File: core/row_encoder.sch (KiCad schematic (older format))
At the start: 16 parts

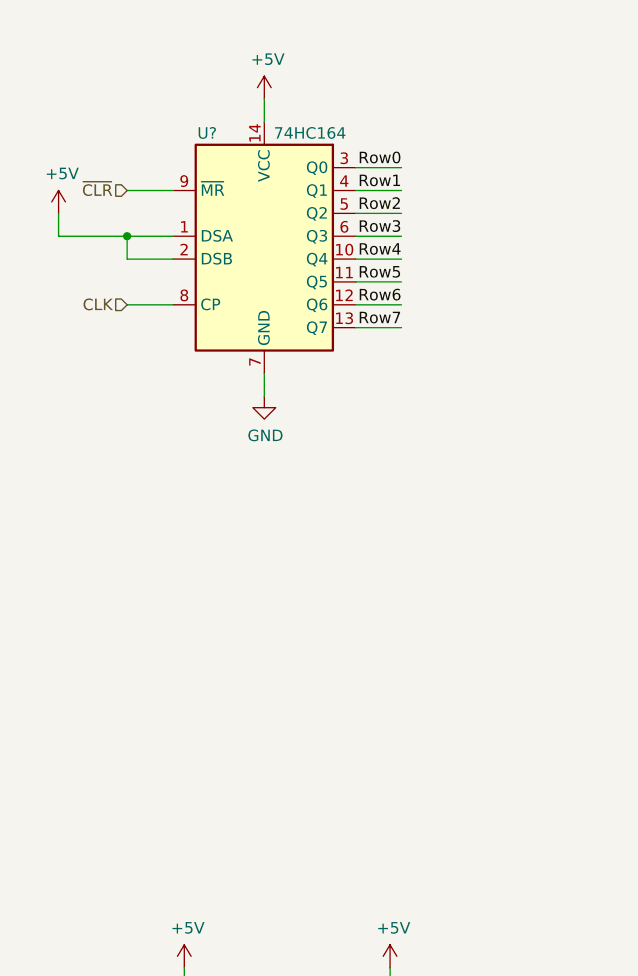
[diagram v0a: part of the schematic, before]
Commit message: Added NOR gate to shift register input to create a ring counter
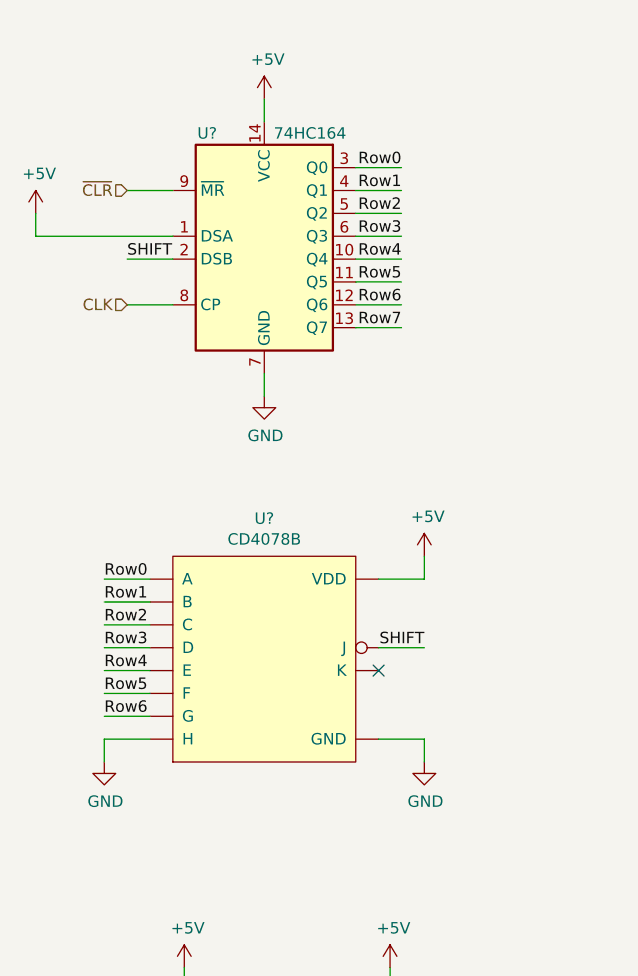
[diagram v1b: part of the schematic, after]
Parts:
- added U?: CD4078B, Package_SO:SOIC-14_3.9x8.7mm_P1.27mm, symbol keyboard_project:CD4078B
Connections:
- net +5V: now also U?.14 (VDD); no longer U?.2 (DSB)
- net GND: now also U?.12 (H), U?.7 (GND)
- net Row0: now also U?.2 (A)
- net Row1: now also U?.3 (B)
- net Row2: now also U?.4 (C)
- net Row3: now also U?.5 (D)
- net Row4: now also U?.9 (E)
- net Row5: now also U?.10 (F)
- net Row6: now also U?.11 (G)
- new net SHIFT: U?.13 (J), U?.2 (DSB)
- no-connect marks 6 -> 7
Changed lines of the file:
@@
 Wire Wire Line
 	3000 2900 2800 2900
-Wire Wire Line
-	3000 3100 2800 3100
-Wire Wire Line
-	2800 3100 2800 3200
-Wire Wire Line
-	2800 3200 3000 3200
-Wire Wire Line
-	2800 3100 2500 3100
-Connection ~ 2800 3100
 $Comp
-L power:+5V #PWR?
-U 1 1 5DC980CA
-P 2500 3000
-F 0 "#PWR?" H 2500 2850 50  0001 C CNN
-F 1 "+5V" H 2515 3173 50  0000 C CNN
-F 2 "" H 2500 3000 50  0001 C CNN
-F 3 "" H 2500 3000 50  0001 C CNN
-	1    2500 3000
+L keyboard_project:CD4078B U?
+U 1 1 5DCCD170
+P 3400 4950
+F 0 "U?" H 3400 5565 50  0000 C CNN
+F 1 "CD4078B" H 3400 5474 50  0000 C CNN
+F 2 "Package_SO:SOIC-14_3.9x8.7mm_P1.27mm" H 3400 4350 50  0001 C CNN
+F 3 "https://www.ti.com/lit/ds/symlink/cd4078b.pdf" H 3100 5450 50  0001 C CNN
+	1    3400 4950
 	1    0    0    -1
 $EndComp
 Wire Wire Line
-	2500 3100 2500 3000
+	2900 5200 2700 5200
+Wire Wire Line
+	2900 5100 2700 5100
+Wire Wire Line
+	2900 5000 2700 5000
+Wire Wire Line
+	2900 4900 2700 4900
+Wire Wire Line
+	2900 4800 2700 4800
+Wire Wire Line
+	2900 4700 2700 4700
+Wire Wire Line
+	2900 4600 2700 4600
+Text Label 2700 4600 0    50   ~ 0
+Row0
+Text Label 2700 4700 0    50   ~ 0
+Row1
+Text Label 2700 4800 0    50   ~ 0
+Row2
+Text Label 2700 4900 0    50   ~ 0
+Row3
+Text Label 2700 5000 0    50   ~ 0
+Row4
+Text Label 2700 5100 0    50   ~ 0
+Row5
+Text Label 2700 5200 0    50   ~ 0
+Row6
+Wire Wire Line
+	4100 4600 4100 4500
+Wire Wire Line
+	4100 5300 4100 5400
+NoConn ~ 3900 5000
+Wire Wire Line
+	3900 4900 4100 4900
+Wire Wire Line
+	3900 4600 4100 4600
+Wire Wire Line
+	3900 5300 4100 5300
+$Comp
+L power:+5V #PWR?
+U 1 1 5DCED549
+P 4100 4500
+F 0 "#PWR?" H 4100 4350 50  0001 C CNN
+F 1 "+5V" H 4115 4673 50  0000 C CNN
+F 2 "" H 4100 4500 50  0001 C CNN
+F 3 "" H 4100 4500 50  0001 C CNN
+	1    4100 4500
+	1    0    0    -1
+$EndComp
+$Comp
+L power:GND #PWR?
+U 1 1 5DCF0662
+P 4100 5400
+F 0 "#PWR?" H 4100 5150 50  0001 C CNN
+F 1 "GND" H 4105 5227 50  0000 C CNN
+F 2 "" H 4100 5400 50  0001 C CNN
+F 3 "" H 4100 5400 50  0001 C CNN
+	1    4100 5400
+	1    0    0    -1
+$EndComp
+Text Label 4100 4900 2    50   ~ 0
+SHIFT
+Wire Wire Line
+	2900 5300 2700 5300
+Wire Wire Line
+	2700 5300 2700 5400
+$Comp
+L power:GND #PWR?
+U 1 1 5DCF9F09
+P 2700 5400
+F 0 "#PWR?" H 2700 5150 50  0001 C CNN
+F 1 "GND" H 2705 5227 50  0000 C CNN
+F 2 "" H 2700 5400 50  0001 C CNN
+F 3 "" H 2700 5400 50  0001 C CNN
+	1    2700 5400
+	1    0    0    -1
+$EndComp
+Wire Wire Line
+	3000 3100 2400 3100
+Wire Wire Line
+	2400 3100 2400 3000
+$Comp
+L power:+5V #PWR?
+U 1 1 5DD01300
+P 2400 3000
+F 0 "#PWR?" H 2400 2850 50  0001 C CNN
+F 1 "+5V" H 2415 3173 50  0000 C CNN
+F 2 "" H 2400 3000 50  0001 C CNN
+F 3 "" H 2400 3000 50  0001 C CNN
+	1    2400 3000
+	1    0    0    -1
+$EndComp
+Wire Wire Line
+	3000 3200 2800 3200
+Text Label 2800 3200 0    50   ~ 0
+SHIFT
 $EndSCHEMATC

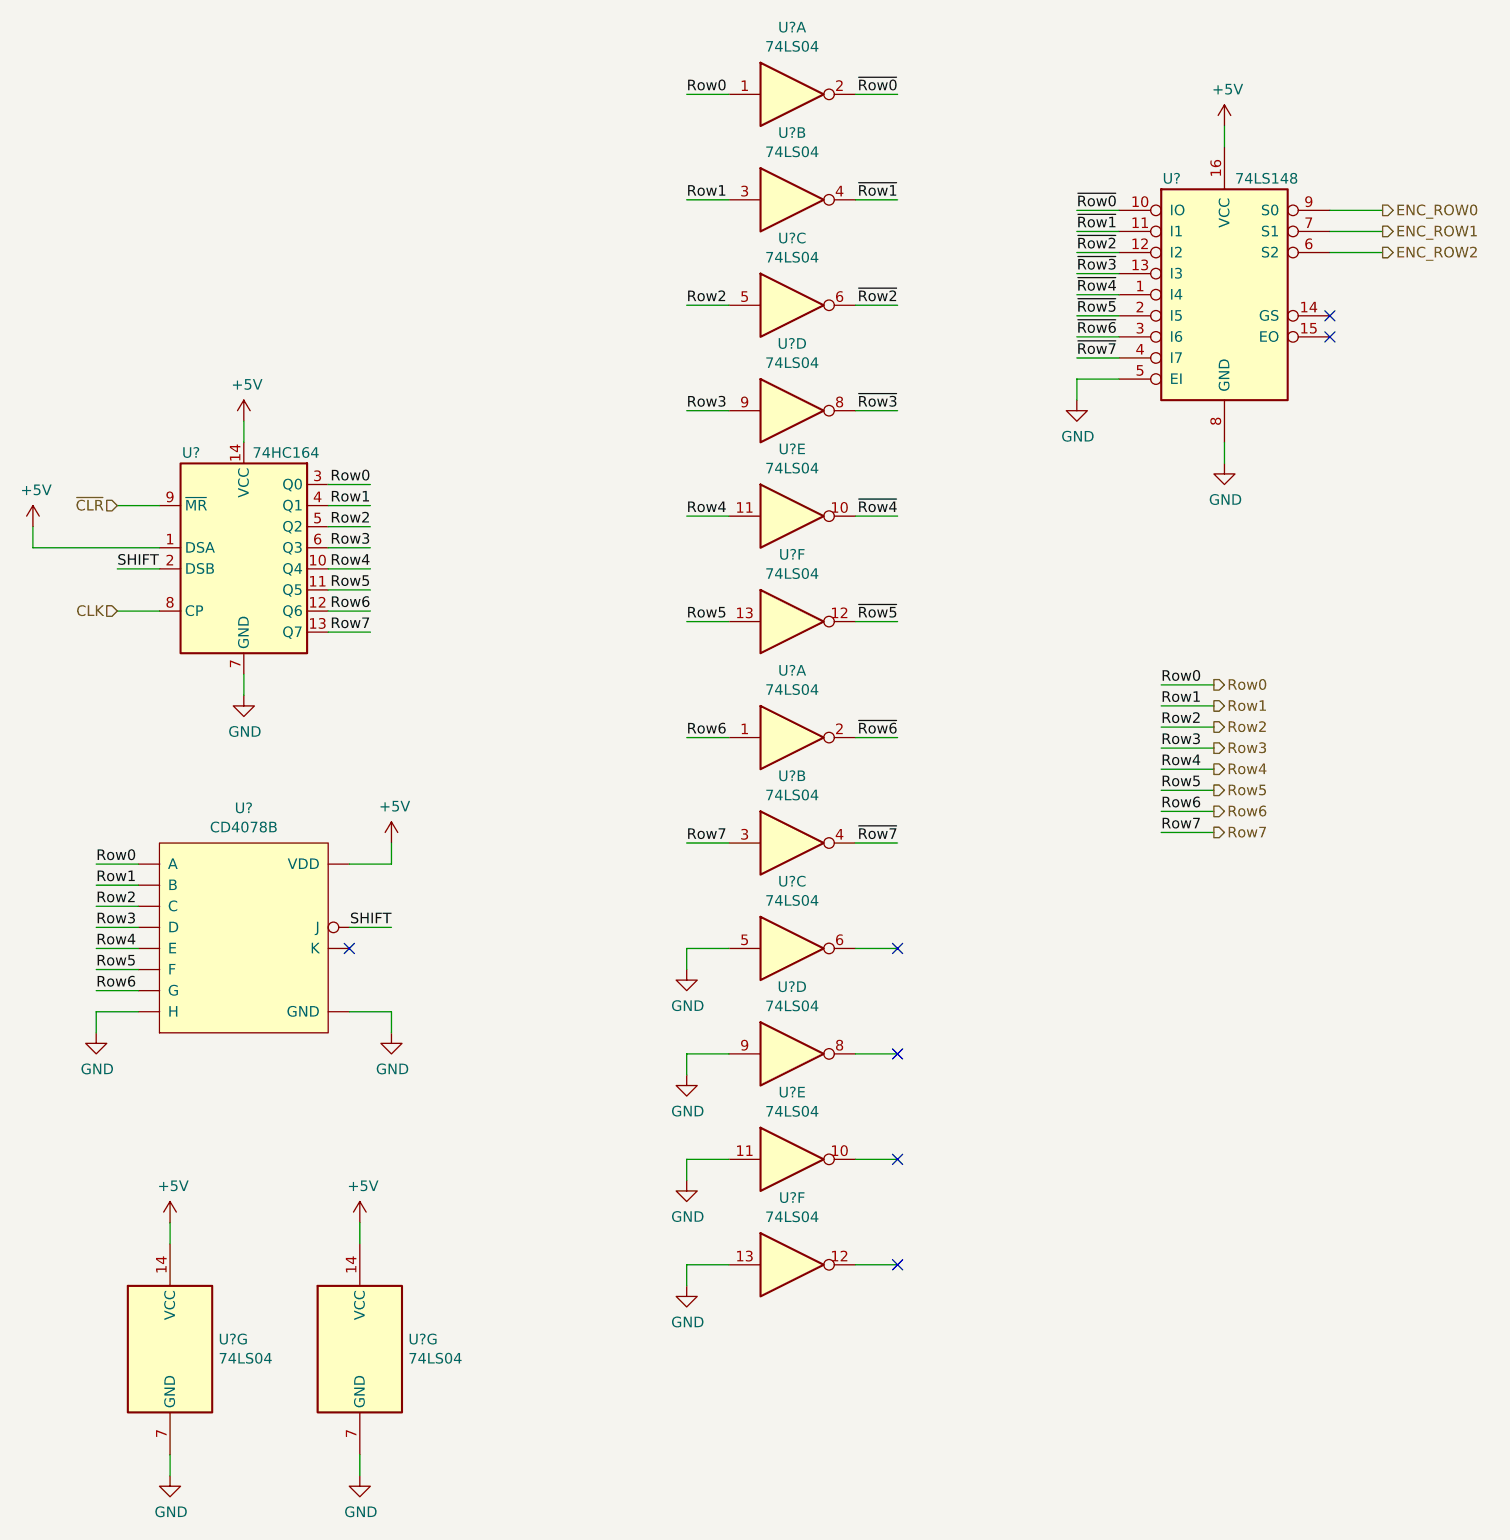
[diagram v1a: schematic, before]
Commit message: Changed encoder to CD4532B, removed inverters
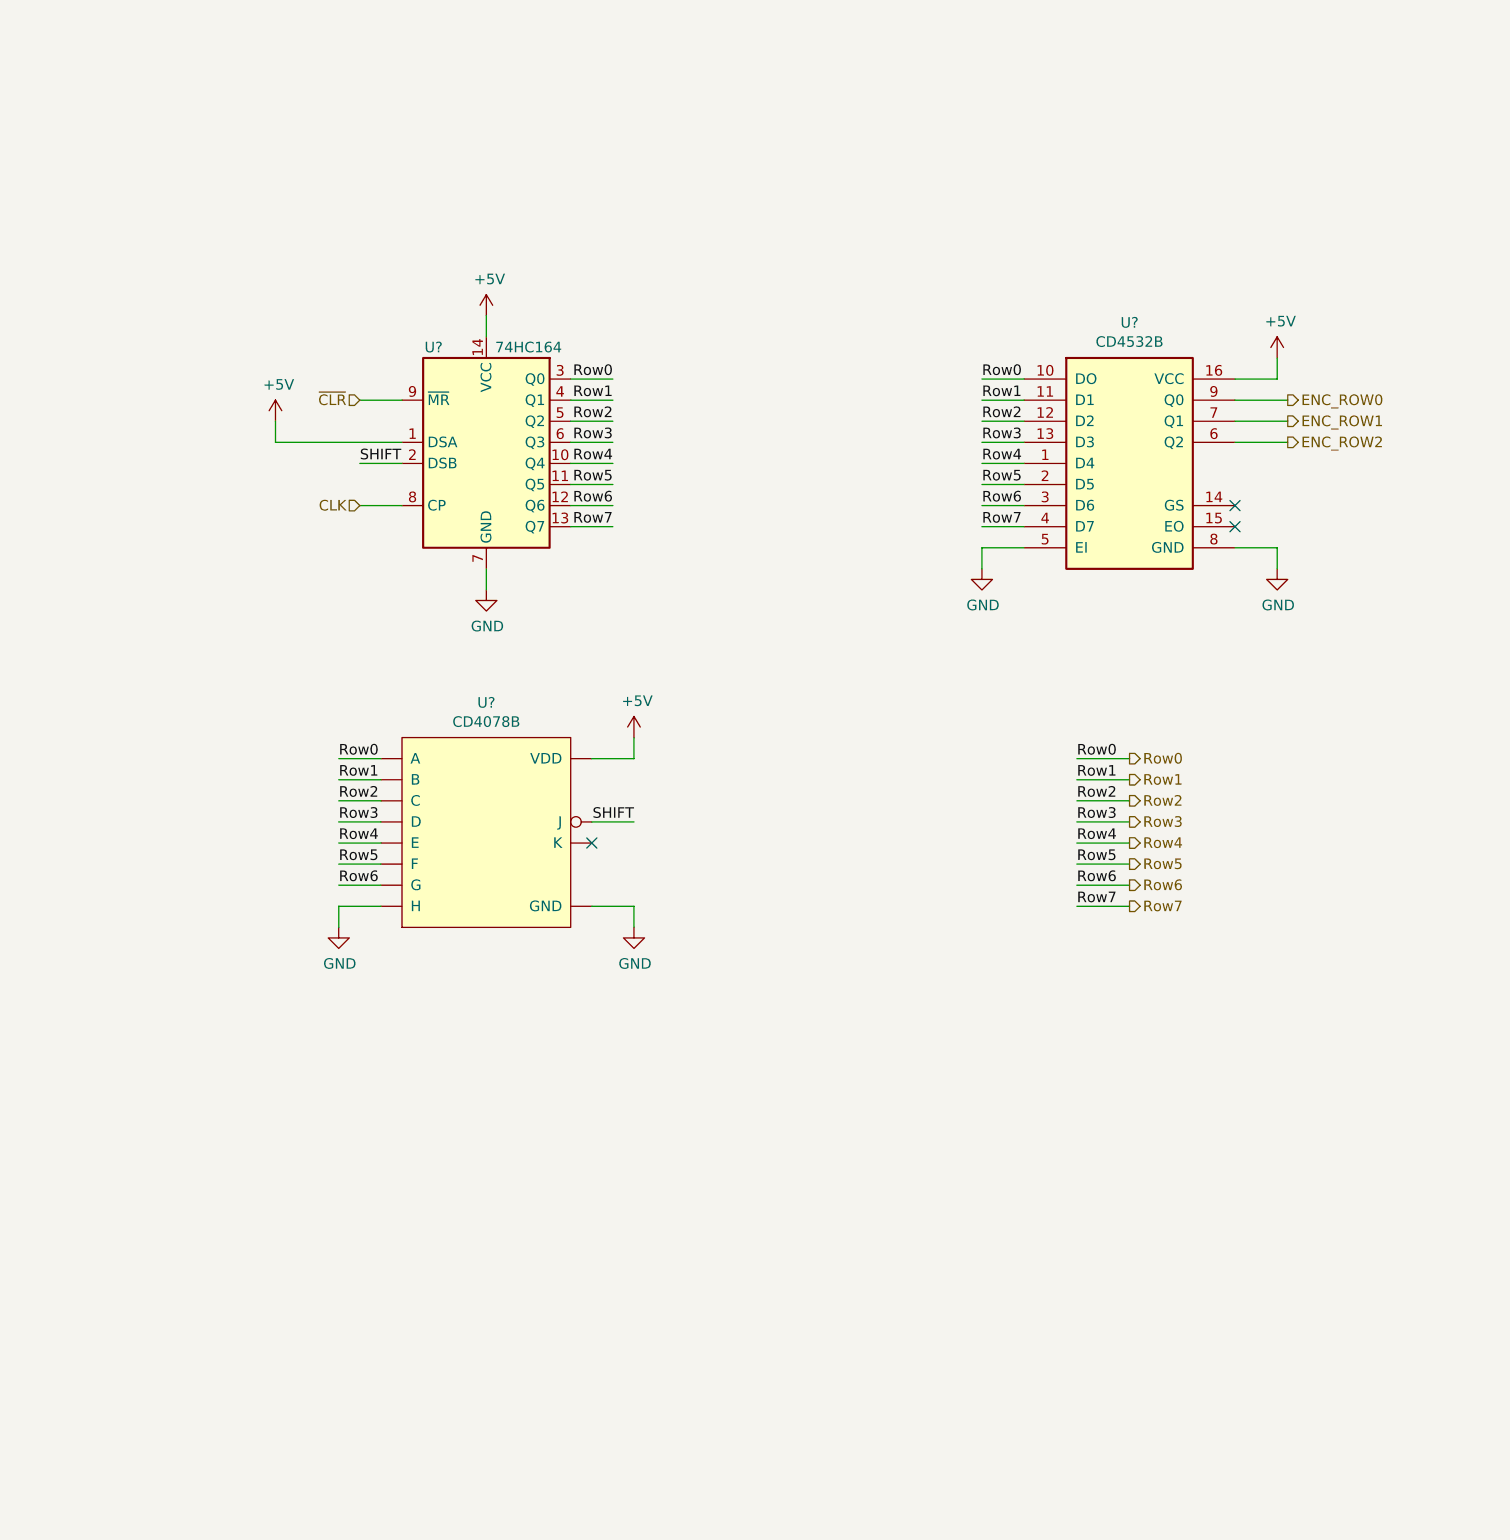
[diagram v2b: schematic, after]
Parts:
- removed U?: 74LS148, symbol 74xx:74LS148
- removed U? (x14): 74LS04, symbol 74xx:74LS04
- added U?: CD4532B, Package_SO:SOIC-14_3.9x8.7mm_P1.27mm, symbol keyboard_project:CD4532B
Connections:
- net +5V: now also U?.16 (VCC)
- net ENC_ROW0: now also U?.9 (Q0)
- net ENC_ROW1: now also U?.7 (Q1)
- net ENC_ROW2: now also U?.6 (Q2)
- net GND: now also U?.5 (EI), U?.8 (GND)
- net Row0: now also U?.10 (DO)
- net Row1: now also U?.11 (D1)
- net Row2: now also U?.12 (D2)
- net Row3: now also U?.13 (D3)
- net Row4: now also U?.1 (D4)
- net Row5: now also U?.2 (D5)
- net Row6: now also U?.3 (D6)
- net Row7: now also U?.4 (D7)
- no-connect marks 7 -> 3
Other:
- moved on the sheet: U?
